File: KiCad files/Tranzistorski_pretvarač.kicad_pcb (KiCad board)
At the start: 2 copper layers, 99.9 x 92.6 mm, 30 parts, among them J1 Screw_Terminal_01x01, J2 Screw_Terminal_01x01, J3 Conn_01x03_Male, J4 Conn_01x01_Male, J5 Screw_Terminal_01x01, J6 Conn_01x01_Male, J7 Conn_01x01_Male, J8 Conn_01x01_Male, J9 Screw_Terminal_01x01, Q1 IRLZ44N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

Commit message: update
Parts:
- added G***: LOGO, footprint:tvz, F.Cu at (149.4, 67.1)
- C5: footprint Capacitor_THT:CP_Radial_D13.0mm_P5.00mm -> Capacitor_THT:CP_Radial_D17.0mm_P7.50mm
- R1: value 1k -> 2k7
- R2: value 3k -> 2k7
- R4: value 2k2 -> 4k7
- R7: value 220 -> 330
- moved C5 0.91 mm to (124.7, 66.7)

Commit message: qr code
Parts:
- added G***: LOGO, footprint:qr, B.Cu at (142.2, 71.2)
- moved R7 10.2 mm to (139.6, 98.9), turned to -90 degrees
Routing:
- net Net-(J6-Pad1): track 73.5 -> 78.4 mm
- net Net-(Q1-Pad1): track 34.5 -> 30.3 mm
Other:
- board text added: "0.47μF"
- board text added: "1μF"
- board text added: "Dokumentacija:"
- board text removed: "0.47u"
- board text removed: "1u"

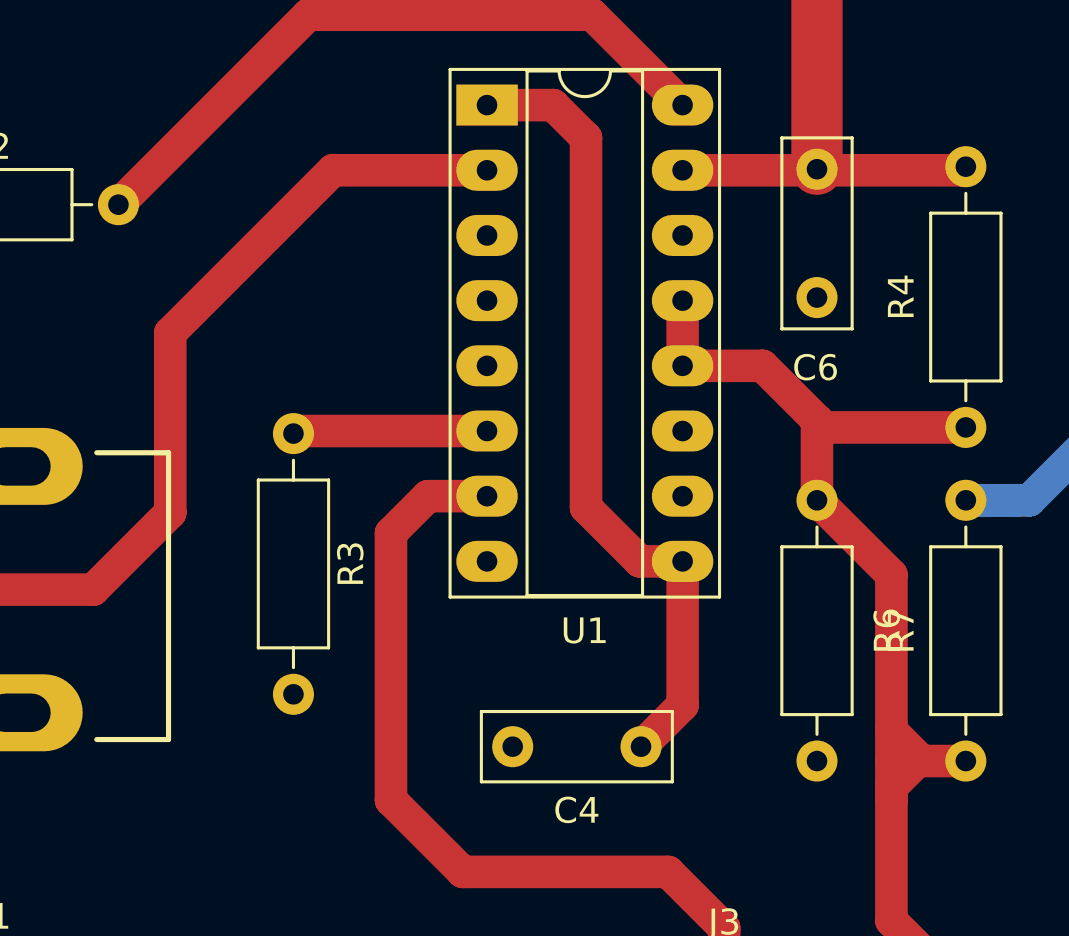
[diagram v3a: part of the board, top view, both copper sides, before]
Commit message: remove copper
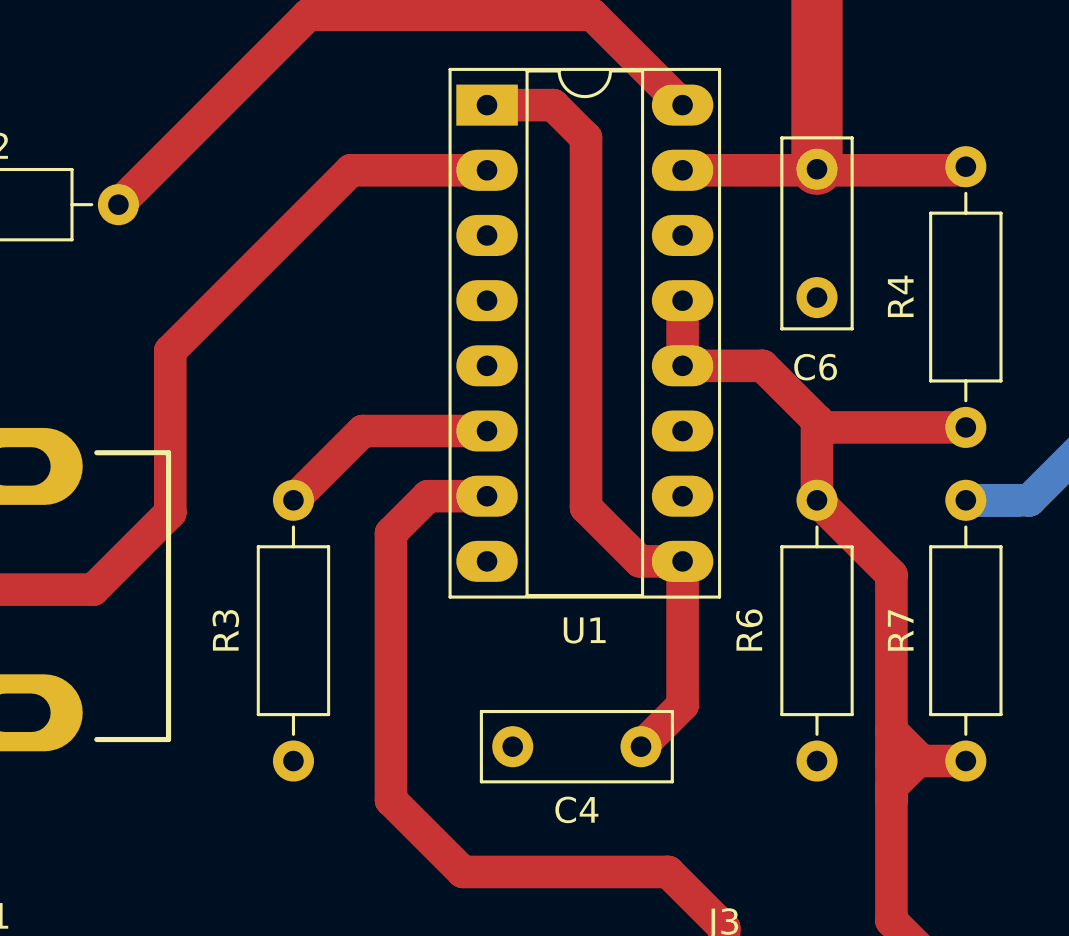
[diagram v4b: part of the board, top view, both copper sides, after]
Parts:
- moved R3 2.60 mm to (113.4, 98.9)
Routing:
- net Net-(R3-Pad1): track 7.58 -> 8.66 mm
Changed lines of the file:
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@@
   )
   (footprint "Resistor_THT:R_Axial_DIN0207_L6.3mm_D2.5mm_P10.16mm_Horizontal" (layer "F.Cu")
-    (at 113.4 96.32 -90)
+    (at 113.4 98.92 -90)
     (descr "Resistor, Axial_DIN0207 series, Axial, Horizontal, pin pitch=10.16mm, 0.25W = 1/4W, length*diameter=6.3*2.5mm^2, http://cdn-reichelt.de/documents/datenblatt/B400/1_4W%23YAG.pdf")
     (tags "Resistor Axial_DIN0207 series Axial Horizontal pin pitch 10.16mm 0.25W = 1/4W length 6.3mm diameter 2.5mm")
@@
     (property "Sheetname" "")
     (attr through_hole)
-    (fp_text reference "R3" (at 5.08 -2.25 90) (layer "F.SilkS")
+    (fp_text reference "R3" (at 5.08 2.6 90) (layer "F.SilkS")
       (effects (font (size 1 1) (thickness 0.15)))
     )
@@
     (property "Sheetname" "")
     (attr through_hole)
-    (fp_text reference "R6" (at 5.08 -2.75 90) (layer "F.SilkS")
+    (fp_text reference "R6" (at 5.08 2.6 90) (layer "F.SilkS")
       (effects (font (size 1 1) (thickness 0.15)))
     )
@@
   (segment (start 96.42 87.4) (end 96.42 99.1695) (width 1.27) (layer "F.Cu") (net 9))
   (segment (start 96.42 99.1695) (end 95.6895 99.9) (width 1.27) (layer "F.Cu") (net 9))
-  (segment (start 120.943 96.22) (end 113.5 96.22) (width 1.27) (layer "F.Cu") (net 10))
-  (segment (start 113.5 96.22) (end 113.4 96.32) (width 1.27) (layer "F.Cu") (net 10))
-  (segment (start 108.6 99.4) (end 108.6 92.4) (width 1.27) (layer "F.Cu") (net 15))
-  (segment (start 114.94 86.06) (end 120.943 86.06) (width 1.27) (layer "F.Cu") (net 15))
+  (segment (start 113.4 98.92) (end 116.1 96.22) (width 1.27) (layer "F.Cu") (net 10))
+  (segment (start 116.1 96.22) (end 120.943 96.22) (width 1.27) (layer "F.Cu") (net 10))
   (segment (start 105.6 102.4) (end 108.6 99.4) (width 1.27) (layer "F.Cu") (net 15))
-  (segment (start 108.6 92.4) (end 114.94 86.06) (width 1.27) (layer "F.Cu") (net 15))
+  (segment (start 108.6 99.4) (end 108.6 93.1) (width 1.27) (layer "F.Cu") (net 15))
   (segment (start 95.6895 102.4) (end 105.6 102.4) (width 1.27) (layer "F.Cu") (net 15))
+  (segment (start 120.943 86.06) (end 115.64 86.06) (width 1.27) (layer "F.Cu") (net 15))
+  (segment (start 115.64 86.06) (end 108.6 93.1) (width 1.27) (layer "F.Cu") (net 15))
   (segment (start 141.48 98.92) (end 141.58 98.92) (width 1.27) (layer "B.Cu") (net 16))
   (segment (start 161.5 95.1) (end 161.5 92.9) (width 1.27) (layer "B.Cu") (net 16))
@@
     )
   )
+  (zone (net 0) (net_name "") (layer "B.Cu") (hatch edge 0.508)
+    (connect_pads (clearance 0))
+    (min_thickness 0.254)
+    (keepout (tracks not_allowed) (vias allowed) (pads allowed ) (copperpour not_allowed) (footprints allowed))
+    (fill (thermal_gap 0.508) (thermal_bridge_width 0.508))
+    (polygon
+      (pts
+        (xy 189 105.2)
+        (xy 175 105.2)
+        (xy 175 75.1)
+        (xy 189 75.1)
+      )
+    )
+  )
   (zone (net 6) (net_name "Net-(D2-Pad2)") (layer "B.Cu") (hatch edge 0.508)
     (priority 1)
@@
     (connect_pads (clearance 0))
     (min_thickness 0.254)
-    (keepout (tracks not_allowed) (vias not_allowed) (pads not_allowed ) (copperpour not_allowed) (footprints allowed))
+    (keepout (tracks not_allowed) (vias allowed) (pads allowed ) (copperpour not_allowed) (footprints allowed))
     (fill (thermal_gap 0.508) (thermal_bridge_width 0.508))
     (polygon
@@
     (connect_pads (clearance 0))
     (min_thickness 0.254)
-    (keepout (tracks not_allowed) (vias not_allowed) (pads not_allowed ) (copperpour not_allowed) (footprints allowed))
+    (keepout (tracks not_allowed) (vias allowed) (pads allowed ) (copperpour not_allowed) (footprints allowed))
+    (fill (thermal_gap 0.508) (thermal_bridge_width 0.508))
+    (polygon
+      (pts
+        (xy 188.9 75.2)
+        (xy 160.5 75.2)
+        (xy 160.5 56.6)
+        (xy 164.5 56)
+        (xy 188.9 56)
+      )
+    )
+  )
+  (zone (net 0) (net_name "") (layer "B.Cu") (hatch edge 0.508)
+    (connect_pads (clearance 0))
+    (min_thickness 0.254)
+    (keepout (tracks not_allowed) (vias allowed) (pads allowed ) (copperpour not_allowed) (footprints allowed))
     (fill (thermal_gap 0.508) (thermal_bridge_width 0.508))
     (polygon
@@
     (connect_pads (clearance 0))
     (min_thickness 0.254)
-    (keepout (tracks not_allowed) (vias not_allowed) (pads not_allowed ) (copperpour not_allowed) (footprints allowed))
+    (keepout (tracks not_allowed) (vias allowed) (pads allowed ) (copperpour not_allowed) (footprints allowed))
+    (fill (thermal_gap 0.508) (thermal_bridge_width 0.508))
+    (polygon
+      (pts
+        (xy 117.1 75.8)
+        (xy 88.7 75.8)
+        (xy 88.7 56.6)
+        (xy 117.1 56.6)
+      )
+    )
+  )
+  (zone (net 0) (net_name "") (layer "B.Cu") (hatch edge 0.508)
+    (connect_pads (clearance 0))
+    (min_thickness 0.254)
+    (keepout (tracks not_allowed) (vias allowed) (pads allowed ) (copperpour not_allowed) (footprints allowed))
+    (fill (thermal_gap 0.508) (thermal_bridge_width 0.508))
+    (polygon
+      (pts
+        (xy 164.6 70.2)
+        (xy 113.1 70.2)
+        (xy 113.1 56.6)
+        (xy 164.5 56.6)
+      )
+    )
+  )
+  (zone (net 0) (net_name "") (layer "B.Cu") (hatch edge 0.508)
+    (connect_pads (clearance 0))
+    (min_thickness 0.254)
+    (keepout (tracks not_allowed) (vias allowed) (pads allowed ) (copperpour not_allowed) (footprints allowed))
     (fill (thermal_gap 0.508) (thermal_bridge_width 0.508))
     (polygon
@@
     (connect_pads (clearance 0))
     (min_thickness 0.254)
-    (keepout (tracks not_allowed) (vias not_allowed) (pads not_allowed ) (copperpour not_allowed) (footprints allowed))
+    (keepout (tracks not_allowed) (vias allowed) (pads allowed ) (copperpour not_allowed) (footprints allowed))
     (fill (thermal_gap 0.508) (thermal_bridge_width 0.508))
     (polygon
